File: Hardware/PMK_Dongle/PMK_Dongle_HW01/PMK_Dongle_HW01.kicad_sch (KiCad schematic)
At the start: 33 parts, among them IC1 ESP32-S2FH4, J1 USB_A, U1 MIC5528-3.3YMT-T5, Y1 Crystal_GND24_Small

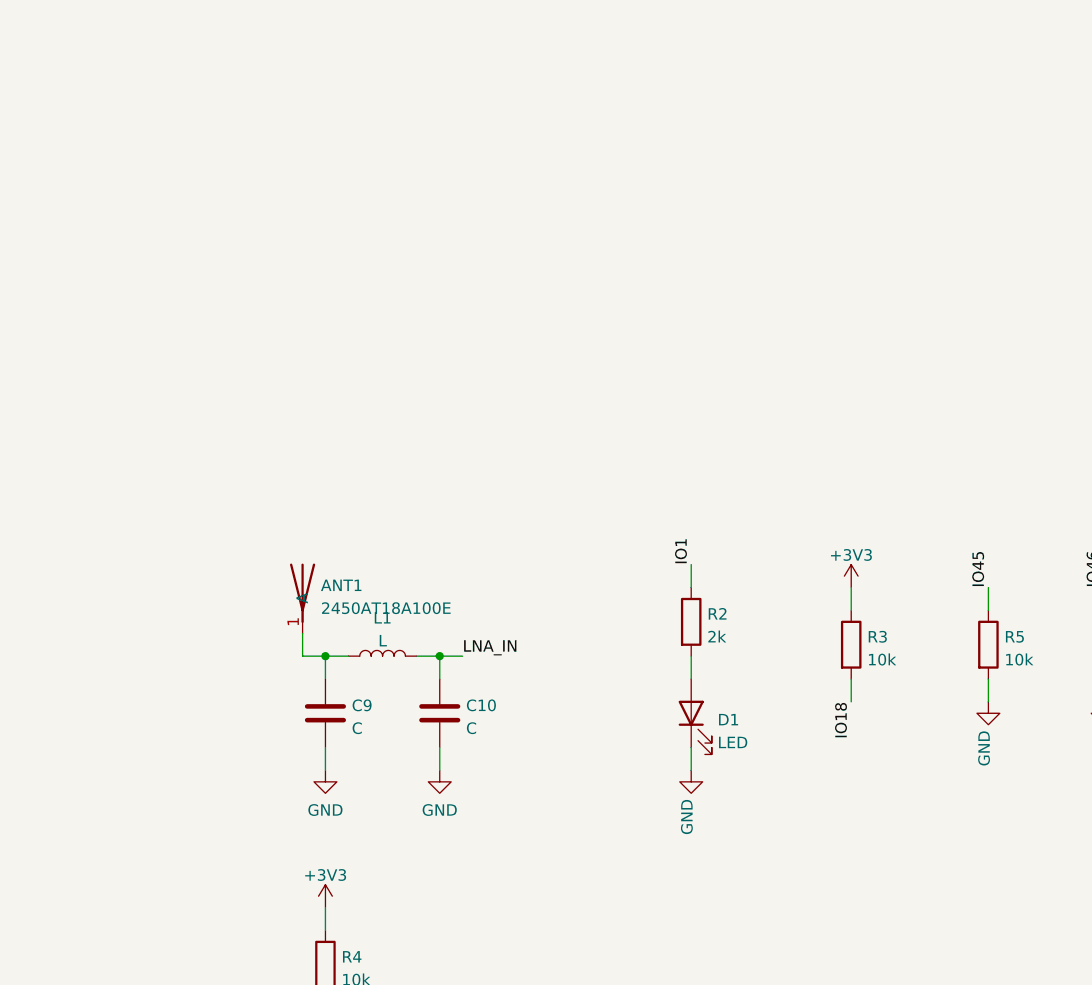
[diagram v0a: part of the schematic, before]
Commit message: working on PMK-dongle_S3 schematic
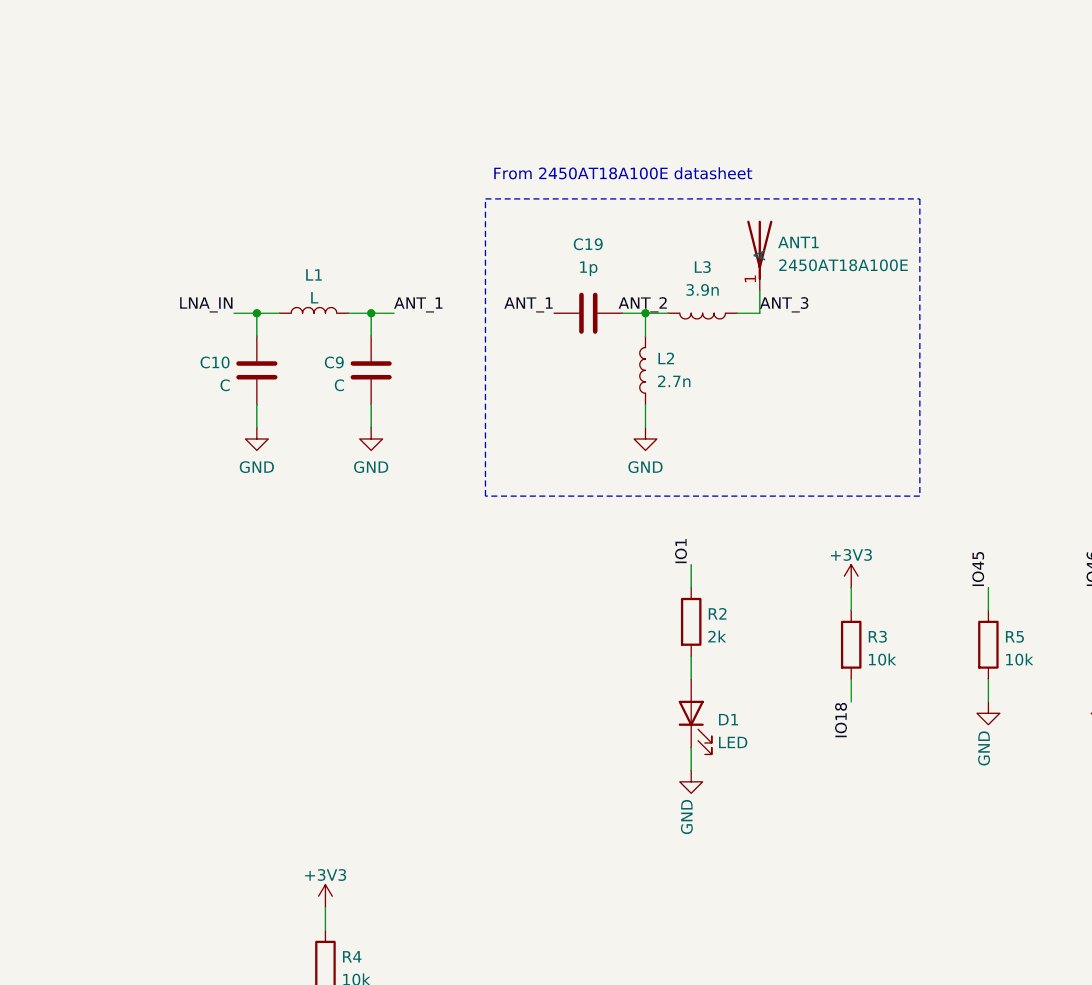
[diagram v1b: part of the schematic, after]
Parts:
- added C19: 1p, Capacitor_SMD:C_0402_1005Metric, symbol Component lib:C
- added L2: 2.7n, Inductor_SMD:L_0402_1005Metric, symbol Component lib:L
- added L3: 3.9n, Inductor_SMD:L_0402_1005Metric, symbol Component lib:L
- R4: footprint Resistor_SMD:R_0402_1005Metric -> Resistor_SMD:R_0201_0603Metric
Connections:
- net GND: now also L2.2
- net ANT_1: now reaches C9.1, L1.1
- net ANT_1: now also C19.2; no longer ANT1.1 (A)
- new net ANT_2: C19.1, L2.1, L3.1
- new net ANT_3: ANT1.1 (A), L3.2
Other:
- note added: "From 2450AT18A100E datasheet"
- moved on the sheet: ANT1, C10, C9, L1
